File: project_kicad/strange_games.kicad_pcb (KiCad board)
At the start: 2 copper layers, 330 x 247.5 mm, 129 parts, among them J1 Display, M1 Motor_DC, Q1 Si2302A, Q2 Q_Photo, Q3 Si2302A, Q4 Q_Photo, SW10 SW_Push, SW11 SW_Push, SW3 SW_Push, SW4 SW_Push, SW5 SW_Push, SW6 SW_Push, SW7 SW_Push, SW8 SW_Push, SW9 SW_Push, U1 charge controller, U2 boost converter, U3 LDL1117S33R, U4 ESP32-DEVKIT-V1, U5 TMP112xxDRL, U6 vibrating_sensor, U7 LSM6DS3, U8 MQ-135 gas sensor

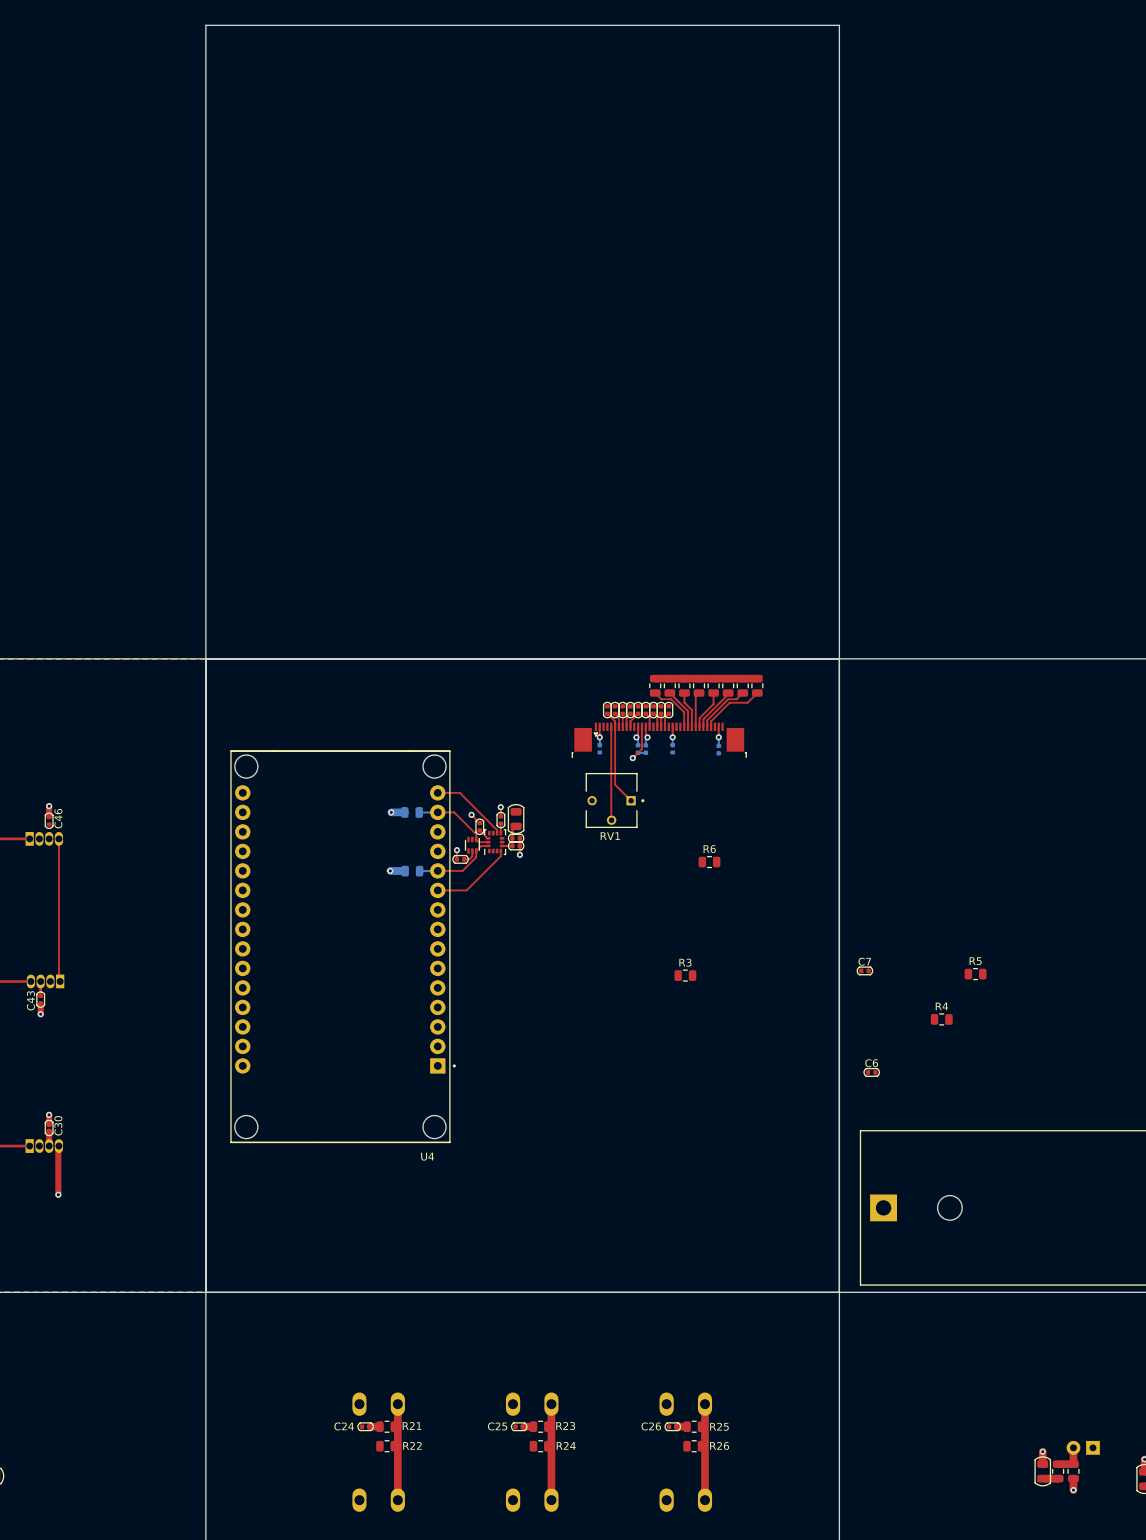
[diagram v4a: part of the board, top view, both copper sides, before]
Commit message: pcb changes
deleted resistor from unused pins because they take so much place
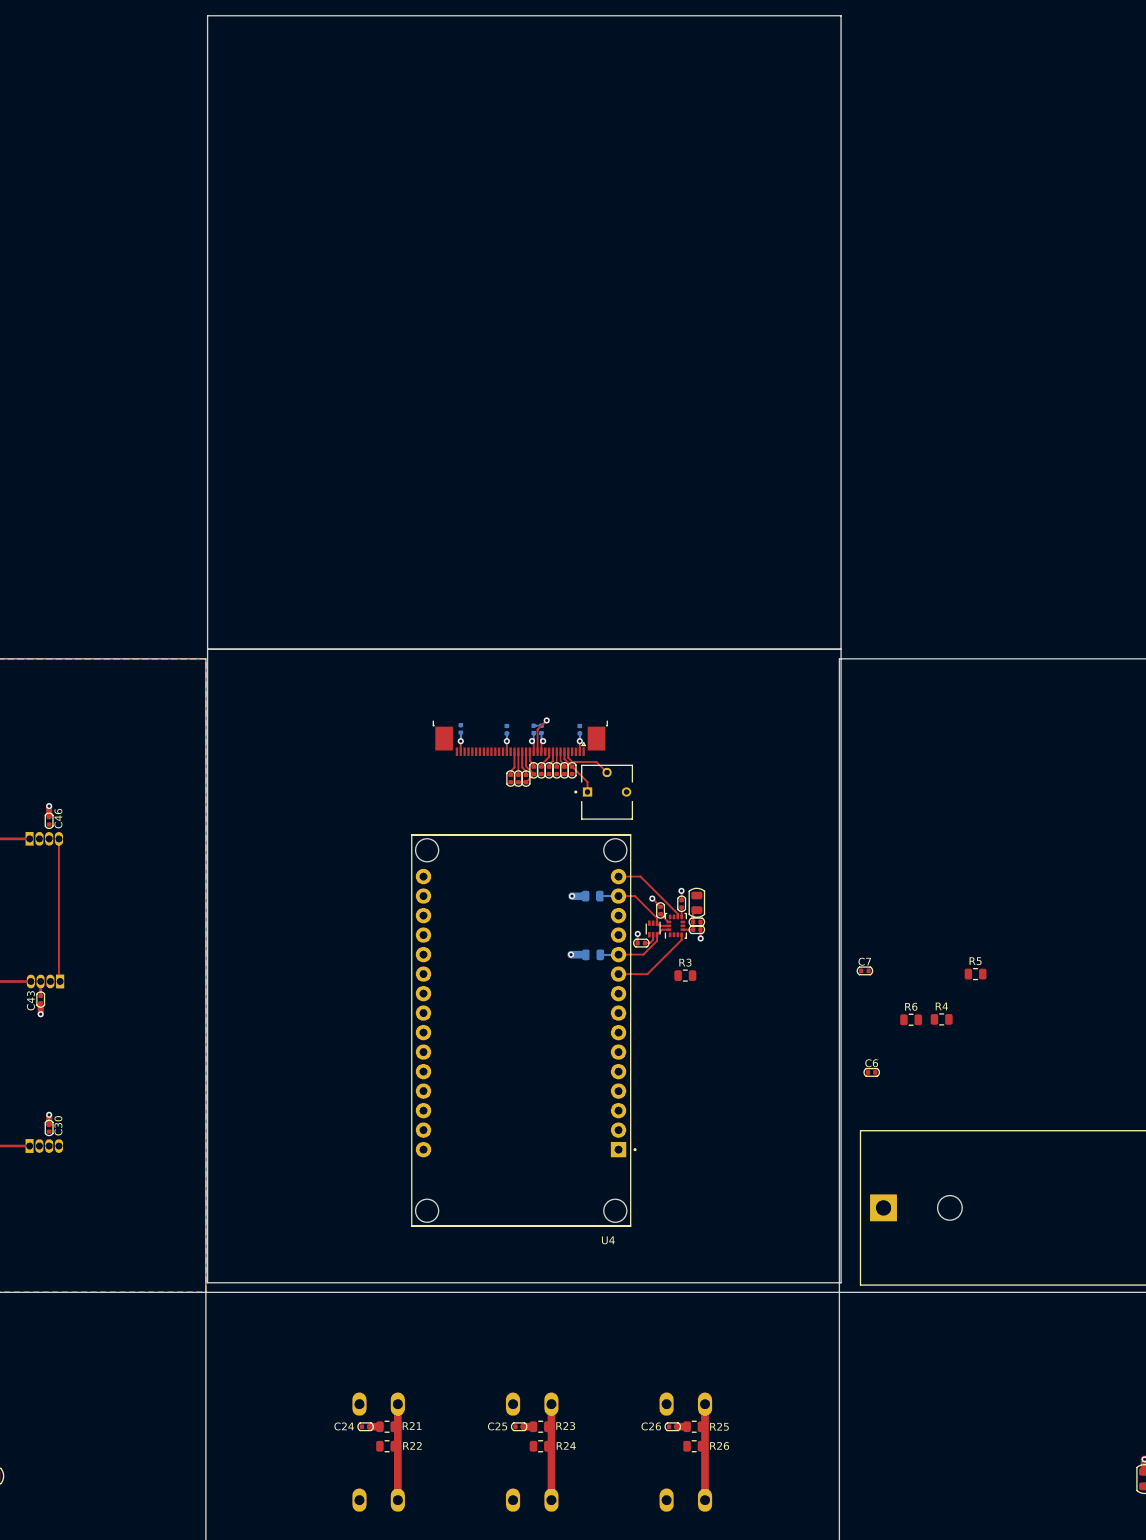
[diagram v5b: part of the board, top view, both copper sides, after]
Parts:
- removed C5: C_Generic, PCM_Capacitor_SMD_AKL:C_0805_2012Metric
- removed Q2: Q_Photo, LED_THT:LED_D4.0mm
- removed R10, R11, R12, R13, R14, R19, R7, R8, R9: 10k_0805, PCM_4ms_Resistor:R_0805_2012Metric
- removed R27: 330_0805, PCM_4ms_Resistor:R_0805_2012Metric
- L1: value L_iron -> L_Iron
- moved C10 33.7 mm to (160.7, 119.1), turned to -90 degrees
- moved R6 33.3 mm to (219.3, 157.0)
- moved C32 25.9 mm to (191.4, 141.8)
- moved C34 25.9 mm to (191.4, 144.3)
- moved C44 25.9 mm to (191.4, 145.3)
- moved R1 25.9 mm to (177.9, 148.6)
- moved C1 25.9 mm to (184.2, 147.0)
- moved C41 25.9 mm to (189.5, 141.9)
- moved C47 25.9 mm to (186.7, 142.8)
- moved R2 25.9 mm to (177.9, 140.9)
- moved U4 25.9 mm to (168.5, 158.4)
- moved U7 25.9 mm to (188.7, 144.8)
- moved U5 25.9 mm to (185.7, 145.2)
- moved C23 22.4 mm to (167.2, 125.6), turned to -90 degrees
- moved C42 21.7 mm to (166.7, 119.2), turned to 90 degrees
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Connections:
- net photo_2 renamed photo
- D3 pad 1: +3V3 -> +12V
- D3 pad 2: Net-(D4-A) -> Net-(D3-A)
- J1 pad 24: Net-(J1-D5) -> +3V3
- J1 pad 25: Net-(J1-D4) -> +3V3
- J1 pad 26: Net-(J1-D3) -> +3V3
- J1 pad 27: Net-(J1-D2) -> +3V3
- J1 pad 28: Net-(J1-D1) -> +3V3
- J1 pad 29: Net-(J1-D0) -> +3V3
- J1 pad 30: Net-(J1-/RD(E)) -> +3V3
- J1 pad 31: Net-(J1-/WR(RW)) -> +3V3
- L1 pad 1: +3V3 -> +12V
- L1 pad 2: Net-(D4-A) -> Net-(D3-A)
- Q1 pad 1: Net-(Q3-G) -> Net-(Q1-G)
- Q1 pad 3: Net-(D4-A) -> Net-(D3-A)
- R15 pad 1: Net-(Q3-G) -> Net-(Q1-G)
- R15 pad 2: vibrating_motor -> open_box
- R16 pad 2: Net-(Q3-G) -> Net-(Q1-G)
- U4 pad 12: photo_1 -> B12
- U5 pad 4: GND -> +3V3
- U7 pad 1: GND -> +3V3
- U7 pad 2: GND -> +3V3
- U7 pad 3: GND -> +3V3
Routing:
- net +3V3: track 68.5 -> 49.5 mm
- net Net-(J1-/WR(RW)): track 8.27 -> 0.00 mm
- net Net-(J1-/RD(E)): track 6.95 -> 0.00 mm
- net Net-(D4-A): track 13.7 -> 6.83 mm
- net Net-(D3-A): track 0.00 -> 6.83 mm
- net Net-(J1-D5): track 6.70 -> 0.00 mm
- net luminodiodes: track 6.37 -> 0.11 mm, vias 1 -> 0
- net Net-(J1-D0): track 6.13 -> 0.00 mm
- net Net-(J1-V0): track 12.6 -> 6.51 mm
- net Net-(J1-VR): track 12.2 -> 6.63 mm
- net Net-(J1-D4): track 5.38 -> 0.00 mm
- net Net-(J1-D1): track 5.16 -> 0.00 mm
- net Net-(J1-D3): track 4.94 -> 0.00 mm
- net Net-(J1-D2): track 4.58 -> 0.00 mm
- net photo_1: track 4.12 -> 0.00 mm
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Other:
- board size 330 x 247.5 mm -> 330 x 248.8 mm
